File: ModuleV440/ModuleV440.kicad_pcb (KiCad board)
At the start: 2 copper layers, 30 x 61.3 mm, 45 parts, among them J2 AVR-ISP-6, Q1 AO3400A, U1 EL3H7(B)(TA)-G, Y1 8MHZ Ceramic Resonator

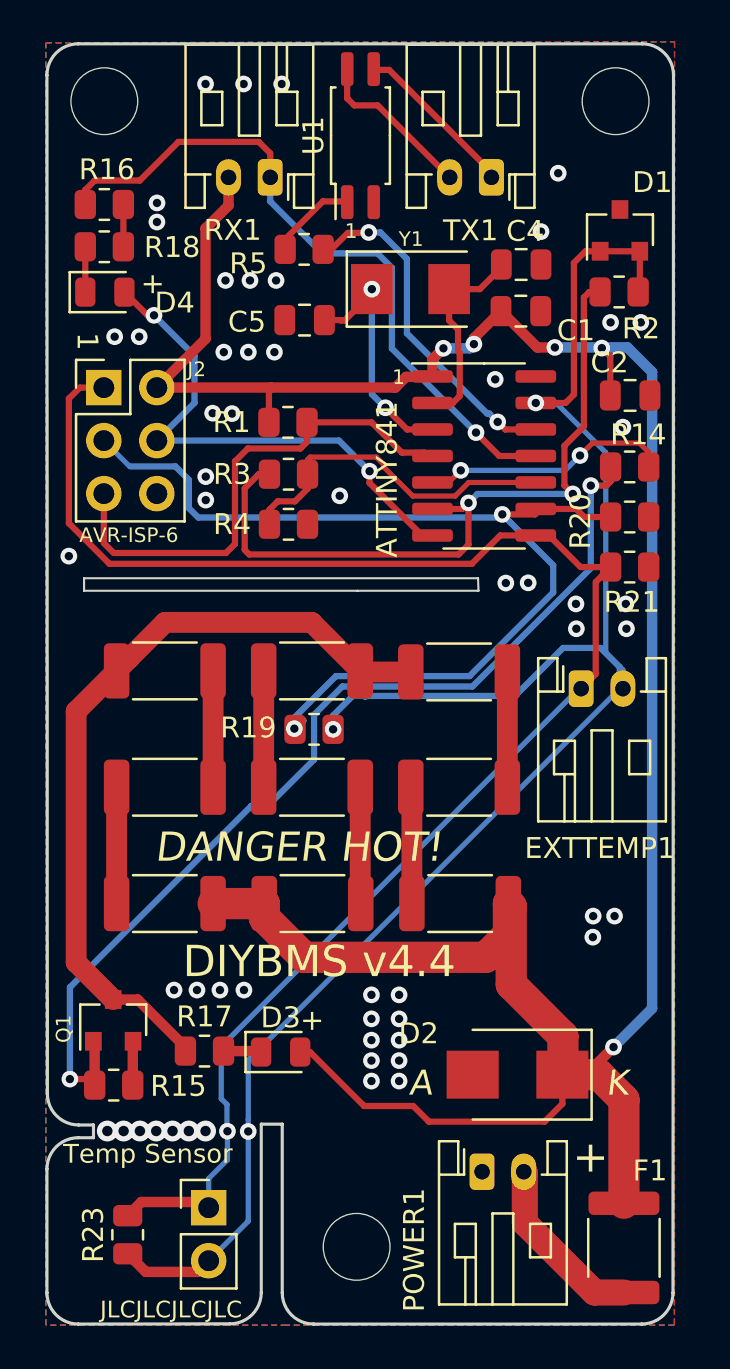
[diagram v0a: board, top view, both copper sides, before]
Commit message: Kicad cleanup, new power dissipation layout (#114)
* Update module v440 to Kicad 6.
* V4.4 PCB design update

Changes:

* reconnect a couple of misaligned vias
* move non-power routes (PTC, bypass switch transistor) off the heat dissipation area
* add a lot of vias and copper to resistor array, for improved heat dissipation
* rearranged resistor array for more connections == larger copper area
* moved the slit up a bit for more room in heat dissipation area
* added "not in schematic" tags to the mount holes

Component values and placement have NOT changed.
(Exception: parts of the resistor array have switched places. That's obviously harmless.)

* Updated for Kicad 6

The schematic has NOT been realigned.

* added "not in schematic" tag to the mounting holes
* Imported V400 to Kicad 6.

The schematic has NOT been realigned.

* added not-in-schematic tags to the mounting holes.
* Minor cleanup
* Switch to kicad 6.0
* Updated date and version#
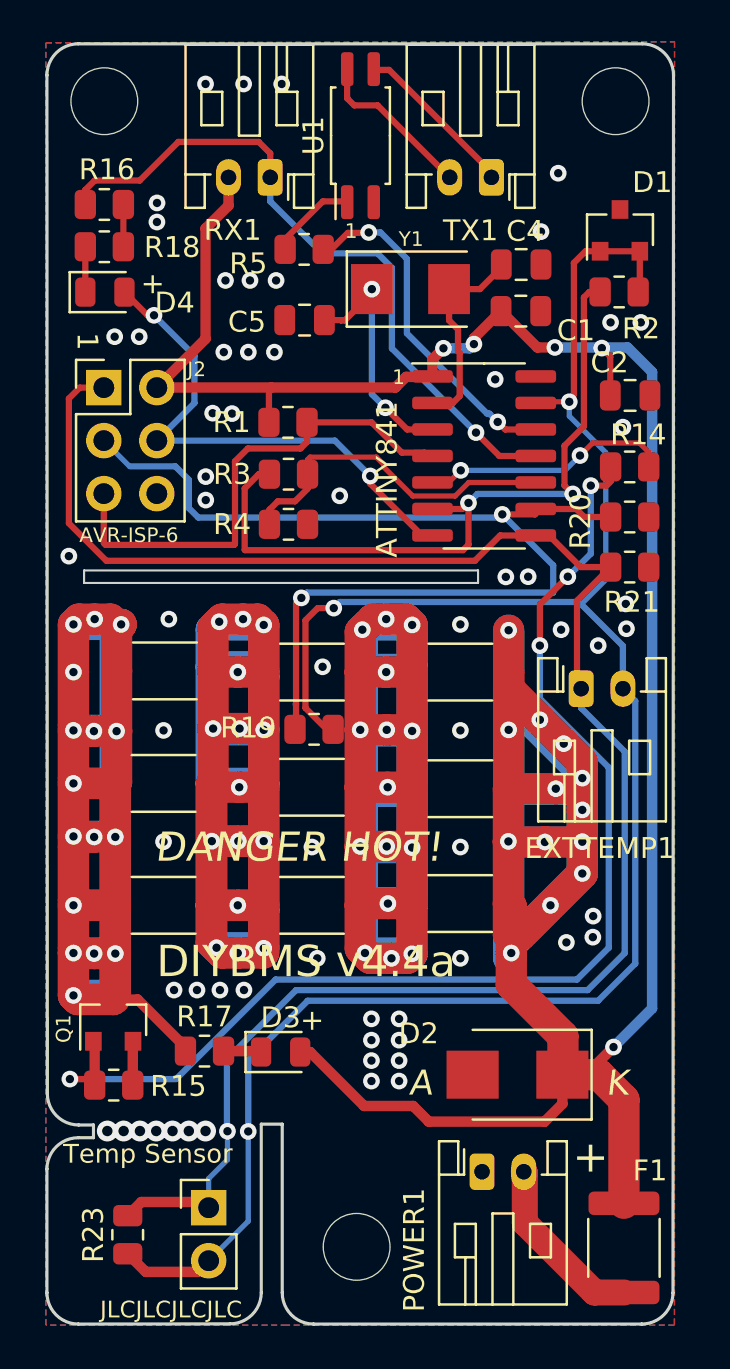
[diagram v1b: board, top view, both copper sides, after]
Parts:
- moved R30 18.0 mm to (107.5, 89.3)
- moved R6 15.2 mm to (121.7, 83.7)
- moved R22 13.2 mm to (121.7, 78.1), turned to 180 degrees
- moved R26 9.04 mm to (114.6, 89.3), turned to 180 degrees
- moved R8 8.95 mm to (114.6, 78.1), turned to 180 degrees
- moved R29 8.92 mm to (107.5, 83.4), turned to 180 degrees
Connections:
- R12 pad 1: Net-(R12-Pad1) -> Net-(R26-Pad2)
- R22 pad 2: Net-(R22-Pad2) -> Net-(R26-Pad1)
- R24 pad 2: Net-(R24-Pad2) -> Net-(R26-Pad1)
- R25 pad 1: Net-(R22-Pad2) -> Net-(R26-Pad1)
- R25 pad 2: Net-(R25-Pad2) -> Net-(R26-Pad2)
- R26 pad 1: Net-(R24-Pad2) -> Net-(R26-Pad1)
- R29 pad 1: Net-(R25-Pad2) -> Net-(R26-Pad2)
- R6 pad 2: Net-(R6-Pad2) -> Net-(R26-Pad1)
- R8 pad 1: Net-(R6-Pad2) -> Net-(R26-Pad1)
- R8 pad 2: Net-(R12-Pad1) -> Net-(R26-Pad2)
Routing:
- net Net-(R26-Pad1): track 0.00 -> 97.6 mm, vias 0 -> 15
- net Net-(R26-Pad2): track 5.53 -> 97.5 mm, vias 0 -> 15
- net Net-(Q1-Pad3): track 37.9 -> 105.9 mm, vias 0 -> 16
- net VCC: track 132.0 -> 190.9 mm, vias 5 -> 18
- net VREF: track 87.6 -> 98.6 mm
- net Net-(Q1-Pad1): track 48.1 -> 58.1 mm, vias 2 -> 4
- net MISO: track 79.1 -> 88.9 mm
- net Net-(R24-Pad2): track 5.60 -> 0.00 mm
- net Net-(R22-Pad2): track 5.59 -> 0.00 mm
- net Net-(R6-Pad2): track 5.58 -> 0.00 mm
- net Net-(R25-Pad2): track 5.58 -> 0.00 mm
- net Net-(R12-Pad1): track 5.58 -> 0.00 mm
- net SCK: track 49.4 -> 51.5 mm
- net GND: vias 48 -> 56
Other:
- outline, holes or cut-outs redrawn
- net class Default removed
- net class Power removed
- board text added: "13 Apr 2022"
- board text added: "DIYBMS v4.4a"
- board text added: "©2019-2022 Stuart Pittaway Matthias Urlichs"
- board text removed: "09 May 2021"
- board text removed: "DIYBMS v4.4"
- board text removed: "©2019-2021 Stuart Pittaway"
